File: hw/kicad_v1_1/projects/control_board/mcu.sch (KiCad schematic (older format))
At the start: 24 parts, among them IC1 ATMEGA168A-A, P2 CONN_02X06, P3 CONN_02X05, SW1 SW_LPH_PUSH, SW2 SW_LPH_PUSH, SW3 SW_LPH_PUSH, SW4 SW_LPH_PUSH

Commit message: Update
Begin work on updating for rev1.1.
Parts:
- R6, R7: value 100 -> 330
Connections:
- net labels added: +5V
- net labels removed: +3.3V
- wire segments 159 -> 155
- no-connect marks 2 -> 6
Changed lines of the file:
@@
 P 4850 5300
 F 0 "R6" V 4900 5100 40  0000 C CNN
-F 1 "100" V 4857 5301 40  0000 C CNN
+F 1 "330" V 4857 5301 40  0000 C CNN
 F 2 "Resistors_SMD:R_0805_HandSoldering" V 4780 5300 30  0001 C CNN
 F 3 "~" H 4850 5300 30  0000 C CNN
@@
 P 4850 5400
 F 0 "R7" V 4900 5200 40  0000 C CNN
-F 1 "100" V 4857 5401 40  0000 C CNN
+F 1 "330" V 4857 5401 40  0000 C CNN
 F 2 "Resistors_SMD:R_0805_HandSoldering" V 4780 5400 30  0001 C CNN
 F 3 "~" H 4850 5400 30  0000 C CNN
@@
 180V_SHTDN
 $Comp
-L SW_LPH_PUSH SW1
-U 1 1 54E28102
-P 3400 5850
-F 0 "SW1" H 3550 5960 50  0000 C CNN
-F 1 "SW_LPH_PUSH" H 3400 5650 50  0000 C CNN
-F 2 "Nixie:FSMRA5JH" H 3950 5900 60  0000 C CNN
-F 3 "" H 3400 5850 60  0000 C CNN
-	1    3400 5850
-	1    0    0    -1
-$EndComp
-$Comp
-L SW_LPH_PUSH SW2
-U 1 1 54E2863D
-P 3400 6350
-F 0 "SW2" H 3550 6460 50  0000 C CNN
-F 1 "SW_LPH_PUSH" H 3400 6150 50  0000 C CNN
-F 2 "Nixie:FSMRA5JH" H 3950 6400 60  0000 C CNN
-F 3 "" H 3400 6350 60  0000 C CNN
-	1    3400 6350
-	1    0    0    -1
-$EndComp
-$Comp
-L SW_LPH_PUSH SW3
-U 1 1 54E2867C
-P 3400 6850
-F 0 "SW3" H 3550 6960 50  0000 C CNN
-F 1 "SW_LPH_PUSH" H 3400 6650 50  0000 C CNN
-F 2 "Nixie:FSMRA5JH" H 3950 6900 60  0000 C CNN
-F 3 "" H 3400 6850 60  0000 C CNN
-	1    3400 6850
-	1    0    0    -1
-$EndComp
-$Comp
-L SW_LPH_PUSH SW4
-U 1 1 54E288B4
-P 3400 7400
-F 0 "SW4" H 3550 7510 50  0000 C CNN
-F 1 "SW_LPH_PUSH" H 3400 7200 50  0000 C CNN
-F 2 "Nixie:FSMRA5JH" H 3950 7450 60  0000 C CNN
-F 3 "" H 3400 7400 60  0000 C CNN
-	1    3400 7400
-	1    0    0    -1
-$EndComp
-$Comp
 L CONN_02X05 P3
 U 1 1 57592C16
@@
 Wire Wire Line
 	3950 4250 5100 4250
-Wire Wire Line
-	3100 5950 3100 5850
-Wire Wire Line
-	3700 5850 3700 5950
-Wire Wire Line
-	3700 6450 3700 6350
-Wire Wire Line
-	3100 6450 3100 6350
-Wire Wire Line
-	3100 6950 3100 6850
-Wire Wire Line
-	3700 6950 3700 6850
-Wire Wire Line
-	3100 7500 3100 7400
-Wire Wire Line
-	3700 7500 3700 7400
 Wire Wire Line
 	6350 2000 7200 2000
@@
 CYA8
 NoConn ~ 1700 6150
-$Comp
-L +3.3V #PWR026
-U 1 1 575E3A22
-P 5800 950
-F 0 "#PWR026" H 5800 800 50  0001 C CNN
-F 1 "+3.3V" H 5800 1090 50  0000 C CNN
-F 2 "" H 5800 950 50  0000 C CNN
-F 3 "" H 5800 950 50  0000 C CNN
-	1    5800 950
-	1    0    0    -1
-$EndComp
-$Comp
-L +3.3V #PWR027
-U 1 1 575E47F2
-P 1000 3000
-F 0 "#PWR027" H 1000 2850 50  0001 C CNN
-F 1 "+3.3V" H 1000 3140 50  0000 C CNN
-F 2 "" H 1000 3000 50  0000 C CNN
-F 3 "" H 1000 3000 50  0000 C CNN
-	1    1000 3000
-	1    0    0    -1
-$EndComp
-$Comp
-L +3.3V #PWR028
-U 1 1 575E4B5E
-P 1100 5850
-F 0 "#PWR028" H 1100 5700 50  0001 C CNN
-F 1 "+3.3V" H 1100 5990 50  0000 C CNN
-F 2 "" H 1100 5850 50  0000 C CNN
-F 3 "" H 1100 5850 50  0000 C CNN
-	1    1100 5850
-	1    0    0    -1
-$EndComp
-$Comp
-L +3.3V #PWR029
-U 1 1 575E53FE
-P 6050 4550
-F 0 "#PWR029" H 6050 4400 50  0001 C CNN
-F 1 "+3.3V" V 6050 4800 50  0000 C CNN
-F 2 "" H 6050 4550 50  0000 C CNN
-F 3 "" H 6050 4550 50  0000 C CNN
-	1    6050 4550
-	0    1    1    0
-$EndComp
-$Comp
-L +3.3V #PWR030
-U 1 1 575E54D0
-P 7750 4450
-F 0 "#PWR030" H 7750 4300 50  0001 C CNN
-F 1 "+3.3V" H 7750 4590 50  0000 C CNN
-F 2 "" H 7750 4450 50  0000 C CNN
-F 3 "" H 7750 4450 50  0000 C CNN
-	1    7750 4450
-	1    0    0    -1
-$EndComp
-$Comp
-L +3.3V #PWR031
-U 1 1 575E55A2
-P 6350 5200
-F 0 "#PWR031" H 6350 5050 50  0001 C CNN
-F 1 "+3.3V" H 6350 5340 50  0000 C CNN
-F 2 "" H 6350 5200 50  0000 C CNN
-F 3 "" H 6350 5200 50  0000 C CNN
-	1    6350 5200
-	1    0    0    -1
-$EndComp
 Wire Wire Line
 	3100 7400 2950 7400
@@
 Wire Wire Line
 	5400 5850 5100 5850
+$Comp
+L +5V #PWR?
+U 1 1 581F1D11
+P 5800 950
+F 0 "#PWR?" H 5800 800 50  0001 C CNN
+F 1 "+5V" H 5800 1090 50  0000 C CNN
+F 2 "" H 5800 950 50  0000 C CNN
+F 3 "" H 5800 950 50  0000 C CNN
+	1    5800 950
+	1    0    0    -1
+$EndComp
+$Comp
+L +5V #PWR?
+U 1 1 581F1DFB
+P 7750 4450
+F 0 "#PWR?" H 7750 4300 50  0001 C CNN
+F 1 "+5V" H 7750 4590 50  0000 C CNN
+F 2 "" H 7750 4450 50  0000 C CNN
+F 3 "" H 7750 4450 50  0000 C CNN
+	1    7750 4450
+	1    0    0    -1
+$EndComp
+$Comp
+L +5V #PWR?
+U 1 1 581F2119
+P 6350 5200
+F 0 "#PWR?" H 6350 5050 50  0001 C CNN
+F 1 "+5V" H 6350 5340 50  0000 C CNN
+F 2 "" H 6350 5200 50  0000 C CNN
+F 3 "" H 6350 5200 50  0000 C CNN
+	1    6350 5200
+	1    0    0    -1
+$EndComp
+$Comp
+L +5V #PWR?
+U 1 1 581F233F
+P 6050 4550
+F 0 "#PWR?" H 6050 4400 50  0001 C CNN
+F 1 "+5V" H 6050 4690 50  0000 C CNN
+F 2 "" H 6050 4550 50  0000 C CNN
+F 3 "" H 6050 4550 50  0000 C CNN
+	1    6050 4550
+	0    1    1    0
+$EndComp
+$Comp
+L +5V #PWR?
+U 1 1 581F26A4
+P 1100 5850
+F 0 "#PWR?" H 1100 5700 50  0001 C CNN
+F 1 "+5V" H 1100 5990 50  0000 C CNN
+F 2 "" H 1100 5850 50  0000 C CNN
+F 3 "" H 1100 5850 50  0000 C CNN
+	1    1100 5850
+	1    0    0    -1
+$EndComp
+$Comp
+L +5V #PWR?
+U 1 1 581F27E8
+P 1000 3000
+F 0 "#PWR?" H 1000 2850 50  0001 C CNN
+F 1 "+5V" H 1000 3140 50  0000 C CNN
+F 2 "" H 1000 3000 50  0000 C CNN
+F 3 "" H 1000 3000 50  0000 C CNN
+	1    1000 3000
+	1    0    0    -1
+$EndComp
+$Comp
+L SW_LPH_PUSH SW4
+U 1 1 54E288B4
+P 3400 7400
+F 0 "SW4" H 3550 7510 50  0000 C CNN
+F 1 "SW_LPH_PUSH" H 3400 7200 50  0000 C CNN
+F 2 "Nixie:FSMRA5JH" H 3950 7450 60  0000 C CNN
+F 3 "" H 3400 7400 60  0000 C CNN
+	1    3400 7400
+	1    0    0    -1
+$EndComp
+$Comp
+L SW_LPH_PUSH SW3
+U 1 1 54E2867C
+P 3400 6850
+F 0 "SW3" H 3550 6960 50  0000 C CNN
+F 1 "SW_LPH_PUSH" H 3400 6650 50  0000 C CNN
+F 2 "Nixie:FSMRA5JH" H 3950 6900 60  0000 C CNN
+F 3 "" H 3400 6850 60  0000 C CNN
+	1    3400 6850
+	1    0    0    -1
+$EndComp
+$Comp
+L SW_LPH_PUSH SW2
+U 1 1 54E2863D
+P 3400 6350
+F 0 "SW2" H 3550 6460 50  0000 C CNN
+F 1 "SW_LPH_PUSH" H 3400 6150 50  0000 C CNN
+F 2 "Nixie:FSMRA5JH" H 3950 6400 60  0000 C CNN
+F 3 "" H 3400 6350 60  0000 C CNN
+	1    3400 6350
+	1    0    0    -1
+$EndComp
+$Comp
+L SW_LPH_PUSH SW1
+U 1 1 54E28102
+P 3400 5850
+F 0 "SW1" H 3550 5960 50  0000 C CNN
+F 1 "SW_LPH_PUSH" H 3400 5650 50  0000 C CNN
+F 2 "Nixie:FSMRA5JH" H 3950 5900 60  0000 C CNN
+F 3 "" H 3400 5850 60  0000 C CNN
+	1    3400 5850
+	1    0    0    -1
+$EndComp
+Wire Wire Line
+	3100 6450 2950 6450
+Connection ~ 2950 6450
+Wire Wire Line
+	3100 5950 2950 5950
+Connection ~ 2950 5950
+Wire Wire Line
+	3100 6950 2950 6950
+Connection ~ 2950 6950
+Wire Wire Line
+	3100 7500 2950 7500
+Connection ~ 2950 7500
+NoConn ~ 3700 5950
+NoConn ~ 3700 6450
+NoConn ~ 3700 6950
+NoConn ~ 3700 7500
 $EndSCHEMATC

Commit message: Schematic Work Complete
Check in schematic work before touching PCB. This should give me a point
to go back to if it all goes to hell.
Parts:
- removed P2: CONN_02X06, Pin_Headers:Pin_Header_Straight_2x06, symbol CONN_02X06
- added P?: CONN_02X05, symbol CONN_02X05
- SW1, SW2, SW3, SW4: symbol SW_LPH_PUSH -> SW_LPH_PUSH-RESCUE-control_board
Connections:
- net labels added: 180V_EN, COL_SEL, N0_A, N0_B, N0_C, N0_D, N1_A, N1_B, N1_C, N1_D, N2_A, N2_B, N2_C, N2_D, N3_A, N3_B, N3_C, N3_D, SEL_N0_A, SEL_N0_B, SEL_N0_C, SEL_N0_D, SEL_N1_A, SEL_N1_B, SEL_N1_C, SEL_N1_D, SEL_N2_A, SEL_N2_B, SEL_N2_C, SEL_N2_D, SEL_N3_A, SEL_N3_B, SEL_N3_C, SEL_N3_D
- net labels removed: 180V_SHTDN, CYA1, D0, D1, DIGIT_SEL, S0, S1, S2, S3, S4, S5, S6, S7, S8, S9, SEL_DOT_BOT, SEL_DOT_TOP, SEL_EIGHT, SEL_FIVE, SEL_FOUR, SEL_NINE, SEL_NIX0, SEL_NIX1, SEL_NIX2, SEL_NIX3, SEL_ONE, SEL_SEVEN, SEL_SIX, SEL_THREE, SEL_TWO, SEL_ZERO, SN0, SN1, SN2, SN3, TUBE_SEL
- wire segments 155 -> 156
- no-connect marks 6 -> 5

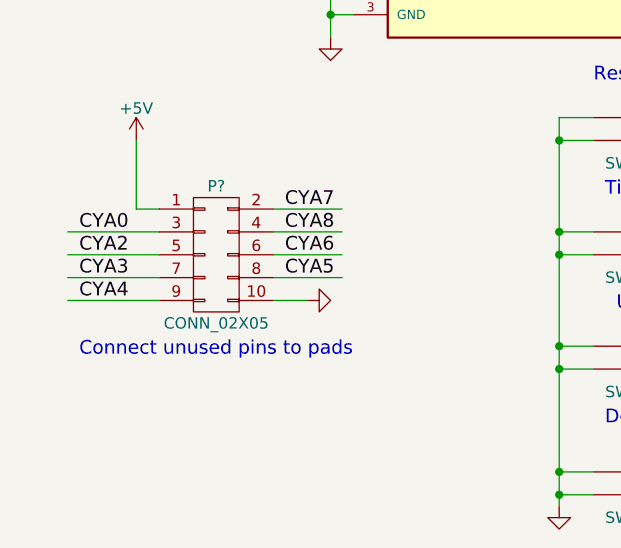
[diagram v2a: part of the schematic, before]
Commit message: Updates to BOM
Start to update BOM for 180V supply
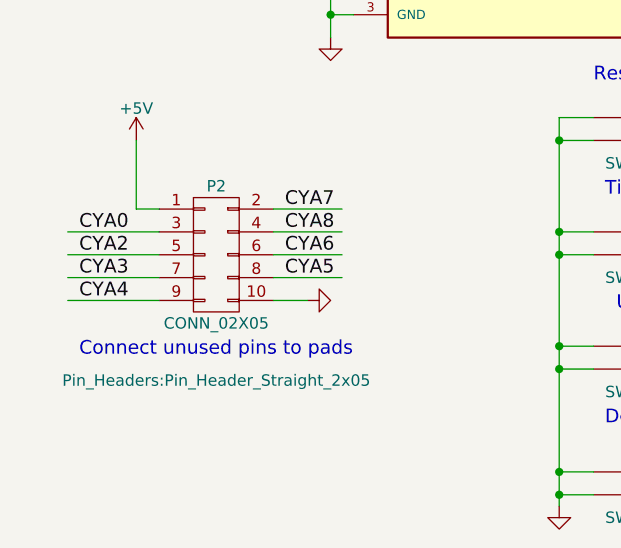
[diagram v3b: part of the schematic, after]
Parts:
- P2: renamed from P?; footprint (none) -> Pin_Headers:Pin_Header_Straight_2x05
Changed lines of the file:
@@
 $EndComp
 $Comp
-L GND #PWR019
+L GND #PWR032
 U 1 1 51B5490A
 P 1000 3650
-F 0 "#PWR019" H 1000 3650 30  0001 C CNN
+F 0 "#PWR032" H 1000 3650 30  0001 C CNN
 F 1 "GND" H 1000 3580 30  0001 C CNN
 F 2 "" H 1000 3650 60  0000 C CNN
@@
 $EndComp
 $Comp
-L GND #PWR020
+L GND #PWR033
 U 1 1 51B54BCA
 P 1750 4200
-F 0 "#PWR020" H 1750 4200 30  0001 C CNN
+F 0 "#PWR033" H 1750 4200 30  0001 C CNN
 F 1 "GND" H 1750 4130 30  0001 C CNN
 F 2 "" H 1750 4200 60  0000 C CNN
@@
 $EndComp
 $Comp
-L GND #PWR021
+L GND #PWR034
 U 1 1 51B54C0E
 P 1950 5500
-F 0 "#PWR021" H 1950 5500 30  0001 C CNN
+F 0 "#PWR034" H 1950 5500 30  0001 C CNN
 F 1 "GND" H 1950 5430 30  0001 C CNN
 F 2 "" H 1950 5500 60  0000 C CNN
@@
 $EndComp
 $Comp
-L GND #PWR022
+L GND #PWR035
 U 1 1 51B58A00
 P 6100 4750
-F 0 "#PWR022" H 6100 4750 30  0001 C CNN
+F 0 "#PWR035" H 6100 4750 30  0001 C CNN
 F 1 "GND" H 6100 4680 30  0001 C CNN
 F 2 "" H 6100 4750 60  0000 C CNN
@@
 $EndComp
 $Comp
-L GND #PWR023
+L GND #PWR036
 U 1 1 51B59B21
 P 2950 7550
-F 0 "#PWR023" H 2950 7550 30  0001 C CNN
+F 0 "#PWR036" H 2950 7550 30  0001 C CNN
 F 1 "GND" H 2950 7480 30  0001 C CNN
 F 2 "" H 2950 7550 60  0000 C CNN
@@
 $EndComp
 $Comp
-L GND #PWR024
+L GND #PWR037
 U 1 1 5759B293
 P 6000 2050
-F 0 "#PWR024" H 6000 2050 30  0001 C CNN
+F 0 "#PWR037" H 6000 2050 30  0001 C CNN
 F 1 "GND" H 6000 1980 30  0001 C CNN
 F 2 "" H 6000 2050 60  0000 C CNN
@@
 Connect unused pins to pads
 $Comp
-L GND #PWR025
+L GND #PWR038
 U 1 1 575D8FF3
 P 1850 6650
-F 0 "#PWR025" H 1850 6650 30  0001 C CNN
+F 0 "#PWR038" H 1850 6650 30  0001 C CNN
 F 1 "GND" H 1850 6580 30  0001 C CNN
 F 2 "" H 1850 6650 60  0000 C CNN
@@
 	5400 5850 5100 5850
 $Comp
-L +5V #PWR?
+L +5V #PWR039
 U 1 1 581F1D11
 P 5800 950
-F 0 "#PWR?" H 5800 800 50  0001 C CNN
+F 0 "#PWR039" H 5800 800 50  0001 C CNN
 F 1 "+5V" H 5800 1090 50  0000 C CNN
 F 2 "" H 5800 950 50  0000 C CNN
@@
 $EndComp
 $Comp
-L +5V #PWR?
+L +5V #PWR040
 U 1 1 581F1DFB
 P 7750 4450
-F 0 "#PWR?" H 7750 4300 50  0001 C CNN
+F 0 "#PWR040" H 7750 4300 50  0001 C CNN
 F 1 "+5V" H 7750 4590 50  0000 C CNN
 F 2 "" H 7750 4450 50  0000 C CNN
@@
 $EndComp
 $Comp
-L +5V #PWR?
+L +5V #PWR041
 U 1 1 581F2119
 P 6350 5200
-F 0 "#PWR?" H 6350 5050 50  0001 C CNN
+F 0 "#PWR041" H 6350 5050 50  0001 C CNN
 F 1 "+5V" H 6350 5340 50  0000 C CNN
 F 2 "" H 6350 5200 50  0000 C CNN
@@
 $EndComp
 $Comp
-L +5V #PWR?
+L +5V #PWR042
 U 1 1 581F233F
 P 6050 4550
-F 0 "#PWR?" H 6050 4400 50  0001 C CNN
+F 0 "#PWR042" H 6050 4400 50  0001 C CNN
 F 1 "+5V" H 6050 4690 50  0000 C CNN
 F 2 "" H 6050 4550 50  0000 C CNN
@@
 $EndComp
 $Comp
-L +5V #PWR?
+L +5V #PWR043
 U 1 1 581F26A4
 P 1100 5950
-F 0 "#PWR?" H 1100 5800 50  0001 C CNN
+F 0 "#PWR043" H 1100 5800 50  0001 C CNN
 F 1 "+5V" H 1100 6090 50  0000 C CNN
 F 2 "" H 1100 5950 50  0000 C CNN
@@
 $EndComp
 $Comp
-L +5V #PWR?
+L +5V #PWR044
 U 1 1 581F27E8
 P 1000 3000
-F 0 "#PWR?" H 1000 2850 50  0001 C CNN
+F 0 "#PWR044" H 1000 2850 50  0001 C CNN
 F 1 "+5V" H 1000 3140 50  0000 C CNN
 F 2 "" H 1000 3000 50  0000 C CNN
@@
 COL_SEL
 $Comp
-L CONN_02X05 P?
+L CONN_02X05 P2
 U 1 1 581FC07F
 P 1450 6450
-F 0 "P?" H 1450 6750 50  0000 C CNN
+F 0 "P2" H 1450 6750 50  0000 C CNN
 F 1 "CONN_02X05" H 1450 6150 50  0000 C CNN
-F 2 "" H 1450 5250 50  0000 C CNN
+F 2 "Pin_Headers:Pin_Header_Straight_2x05" H 1450 5900 50  0000 C CNN
 F 3 "" H 1450 5250 50  0000 C CNN
 	1    1450 6450

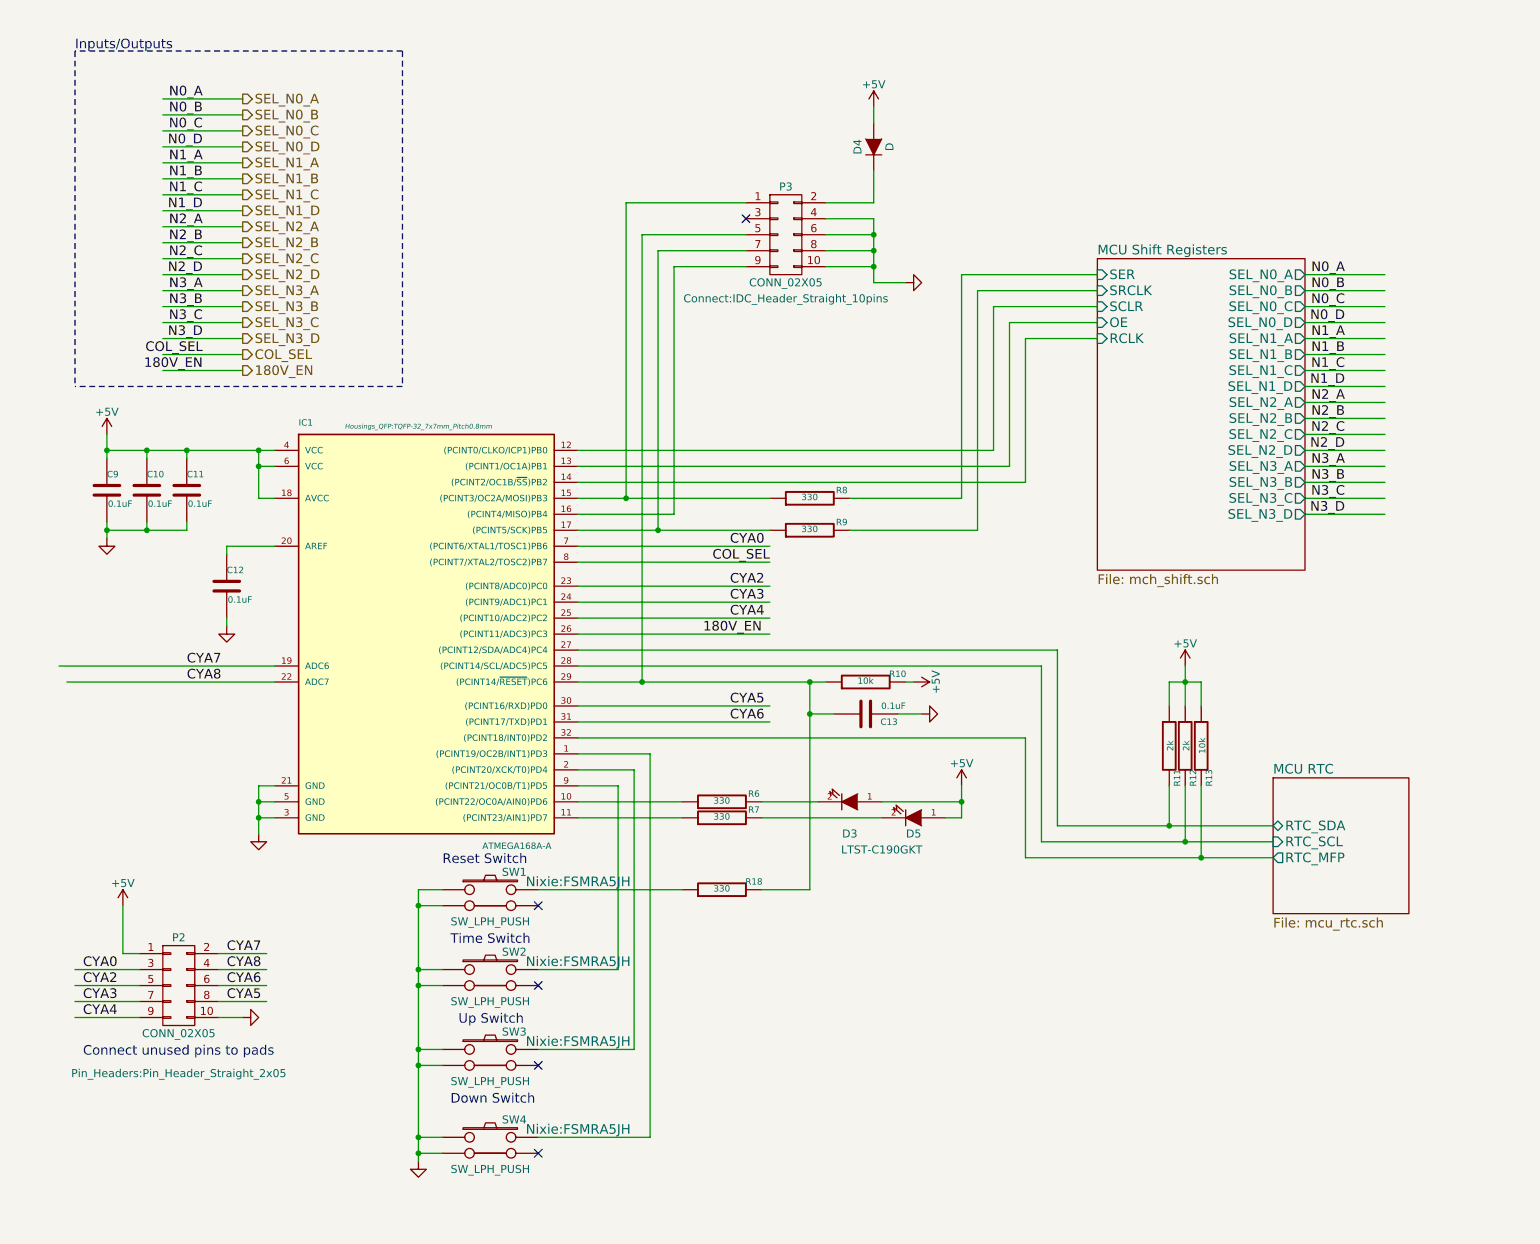
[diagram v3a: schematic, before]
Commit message: Complete with errors
Check in before moving header. Currently the headers don't match up. If
I'm going to connect them with standard header I need to move it
significantly. Check in as a roll back point.
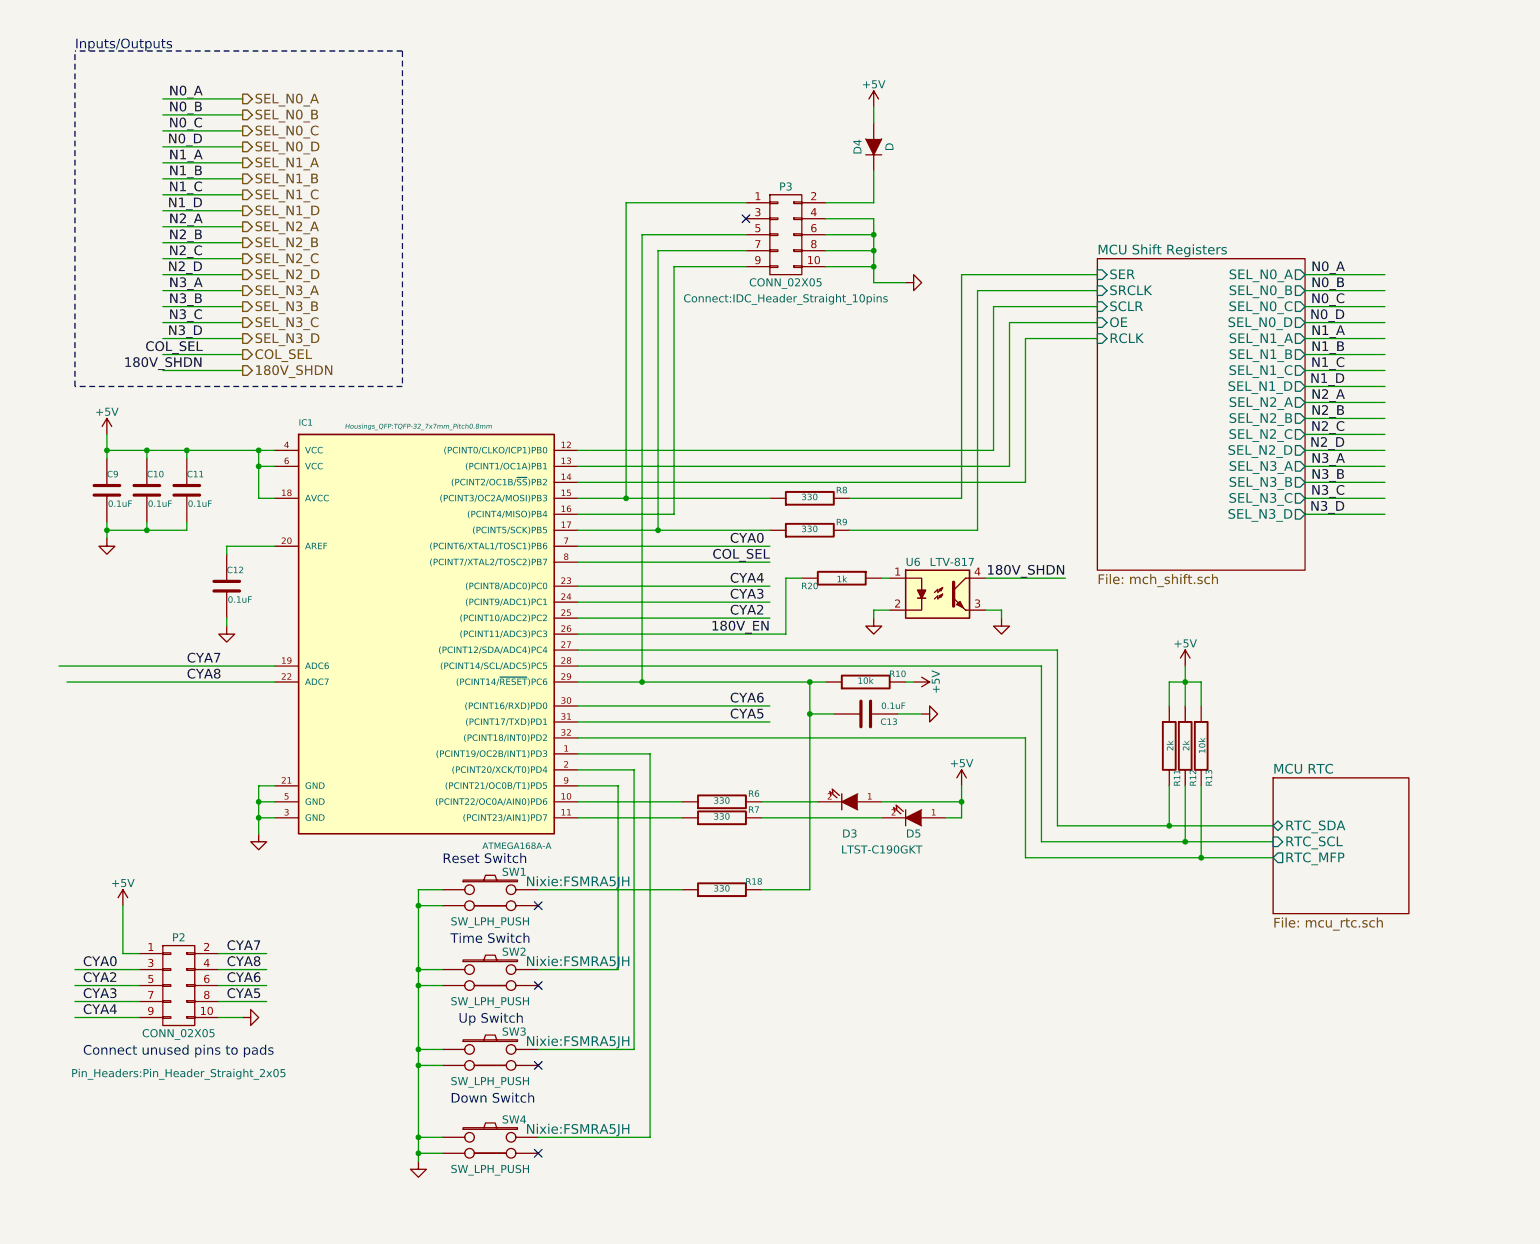
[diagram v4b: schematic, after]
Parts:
- added R20: 1k, Resistors_SMD:R_0805_HandSoldering, symbol R-RESCUE-nixie_clock
- added U6: LTV-817, Opto-Devices:Optocoupler_SMD_LTV-817S, symbol LTV-817
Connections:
- net labels added: 180V_SHDN
- wire segments 156 -> 164
